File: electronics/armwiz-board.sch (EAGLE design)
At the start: 99 parts, among them IC3 SN74LVC1G74DCT, J1 MICRO-SDCARD-CONNECTOR-330006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, Q1 DMP2035U-7, Q2 DMP2035U-7, Q3 DMN2075U-7, Q4 DMN2075U-7, Q5 DMP2035U-7, U1 STM32F10XRXT6, U2 APX809, U3 MCP73831, U4 MIC5219-3.3V, X1 FH12-12S-1S

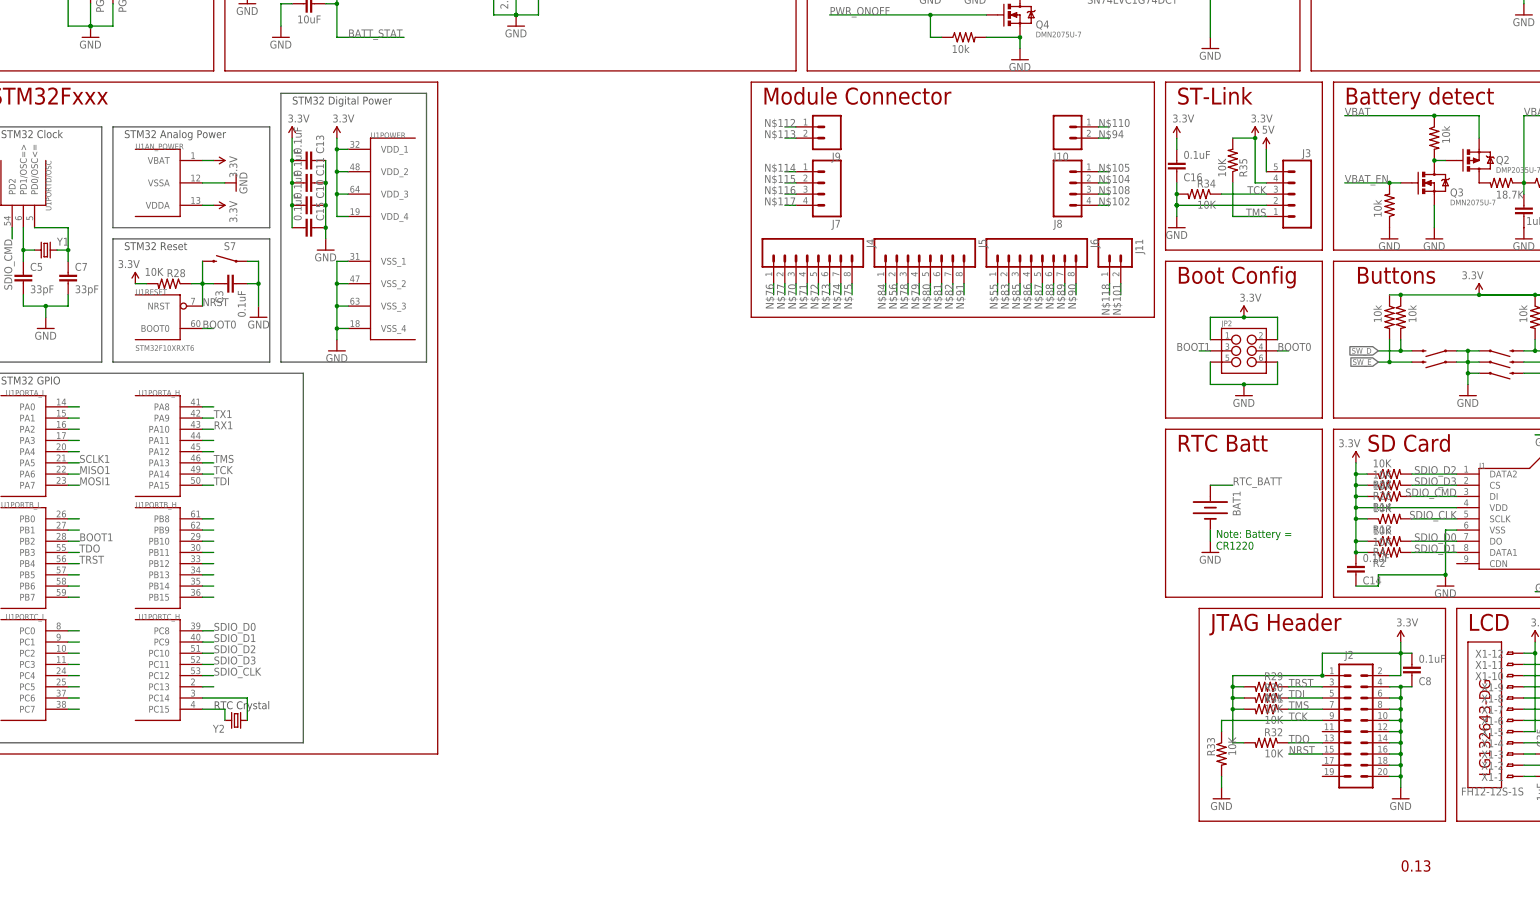
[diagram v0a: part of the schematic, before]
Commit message: Removed JTAG and ST-Link connectors. Added ARM Cortex Debug connector.
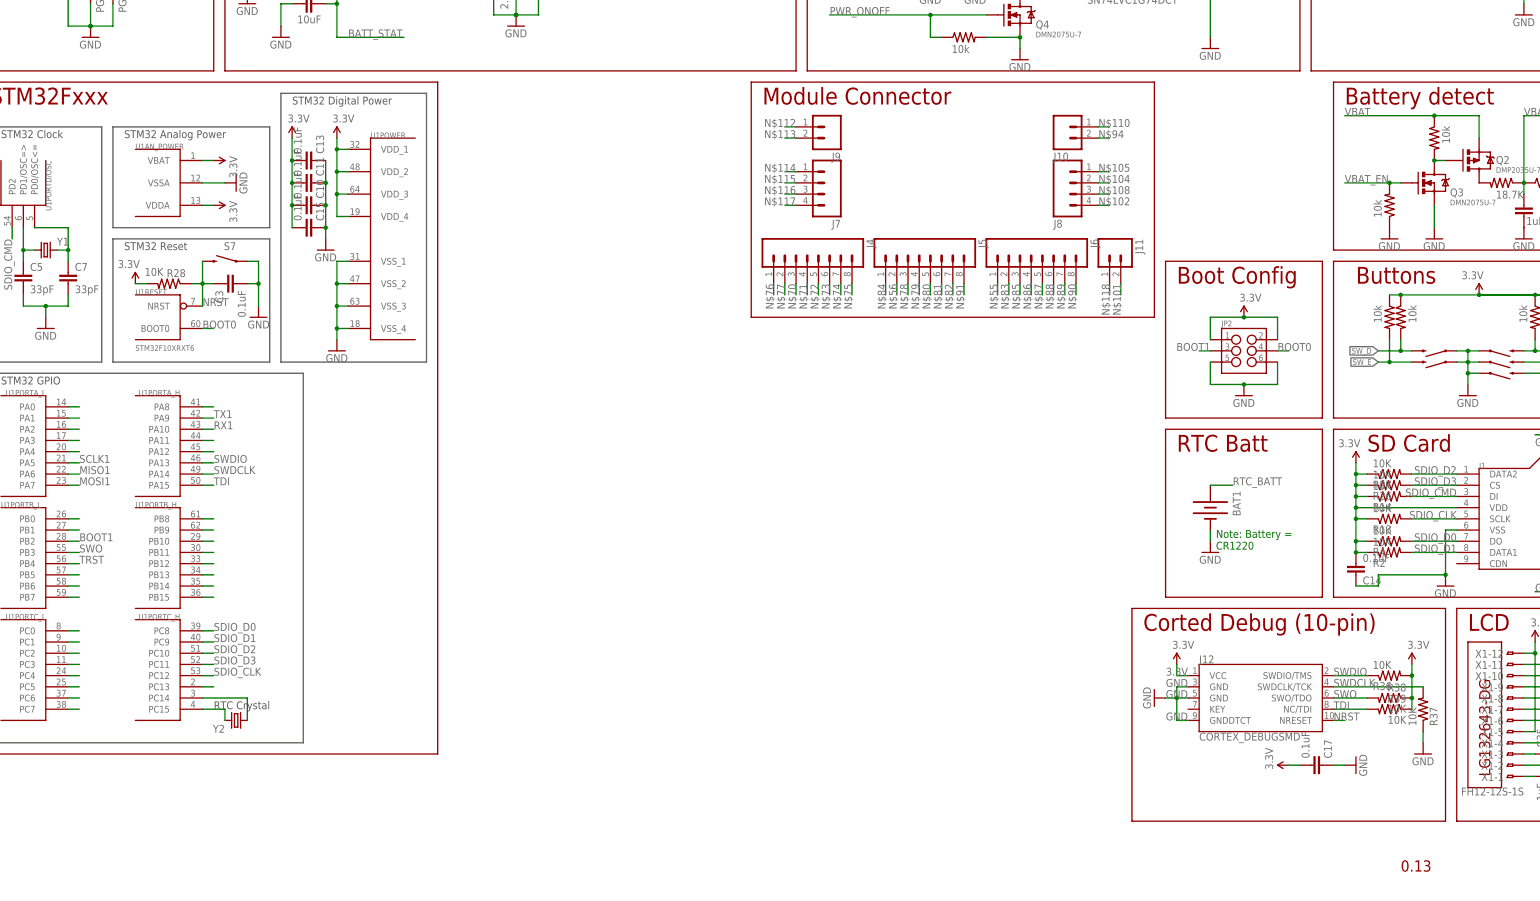
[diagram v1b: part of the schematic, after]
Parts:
- removed C16, C8: 0.1uF, SparkFun-Capacitors:0.1UF-25V-5%(0603)
- removed J2: (no value), SparkFun-Connectors:M10X2
- removed J3: (no value), SparkFun-Connectors:M05PTH
- removed R29, R30, R31, R32, R33, R34, R35: 10K, SparkFun-Resistors:10KOHM-1/10W-1%(0603)0603
- added C17: 0.1uF, SparkFun-Capacitors:0.1UF-25V-5%(0603)
- added J12: CORTEX_DEBUGSMD, SparkFun-Connectors:CORTEX_DEBUGSMD
- added R36, R37, R38, R39: 10K, SparkFun-Resistors:10KOHM-1/10W-1%(0603)0603
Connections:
- removed net 5V: J3.5
- removed net TCK: J2.9, J3.3, R33.1, R34.1, U1PORTA_H.PA14
- removed net TDO: J2.13, R32.1, U1PORTB_L.PB3
- removed net TMS: J2.7, J3.1, R31.1, R35.1, U1PORTA_H.PA13
- new net SWDCLK: J12.SWDCLK/TCK, R37.2, U1PORTA_H.PA14
- new net SWDIO: J12.SWDIO/TMS, R36.1, U1PORTA_H.PA13
- new net SWO: J12.SWO/TDO, R38.2, U1PORTB_L.PB3
- net 3.3V: now also C17.2, J12.VCC, R36.2, R38.1, R39.1; no longer C16.2, C8.2, J2.1, J2.2, J3.4, R29.2, R30.2, R31.2, R32.2, R35.2
- net GND: now also C17.1, J12.GND@3, J12.GND@5, J12.GNDDTCT, R37.1; no longer C16.1, C8.1, J2.10, J2.12, J2.14, J2.16, J2.18, J2.20, J2.4, J2.6, J2.8, J3.2, R33.2, R34.2
- net NRST: now also J12.NRESET; no longer J2.15
- net TDI: now also J12.NC/TDI, R39.2; no longer J2.5, R30.1
- net TRST: no longer J2.3, R29.1
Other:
- note added: "Corted Debug (10-pin)"
- note removed: "JTAG Header"
- note removed: "ST-Link"

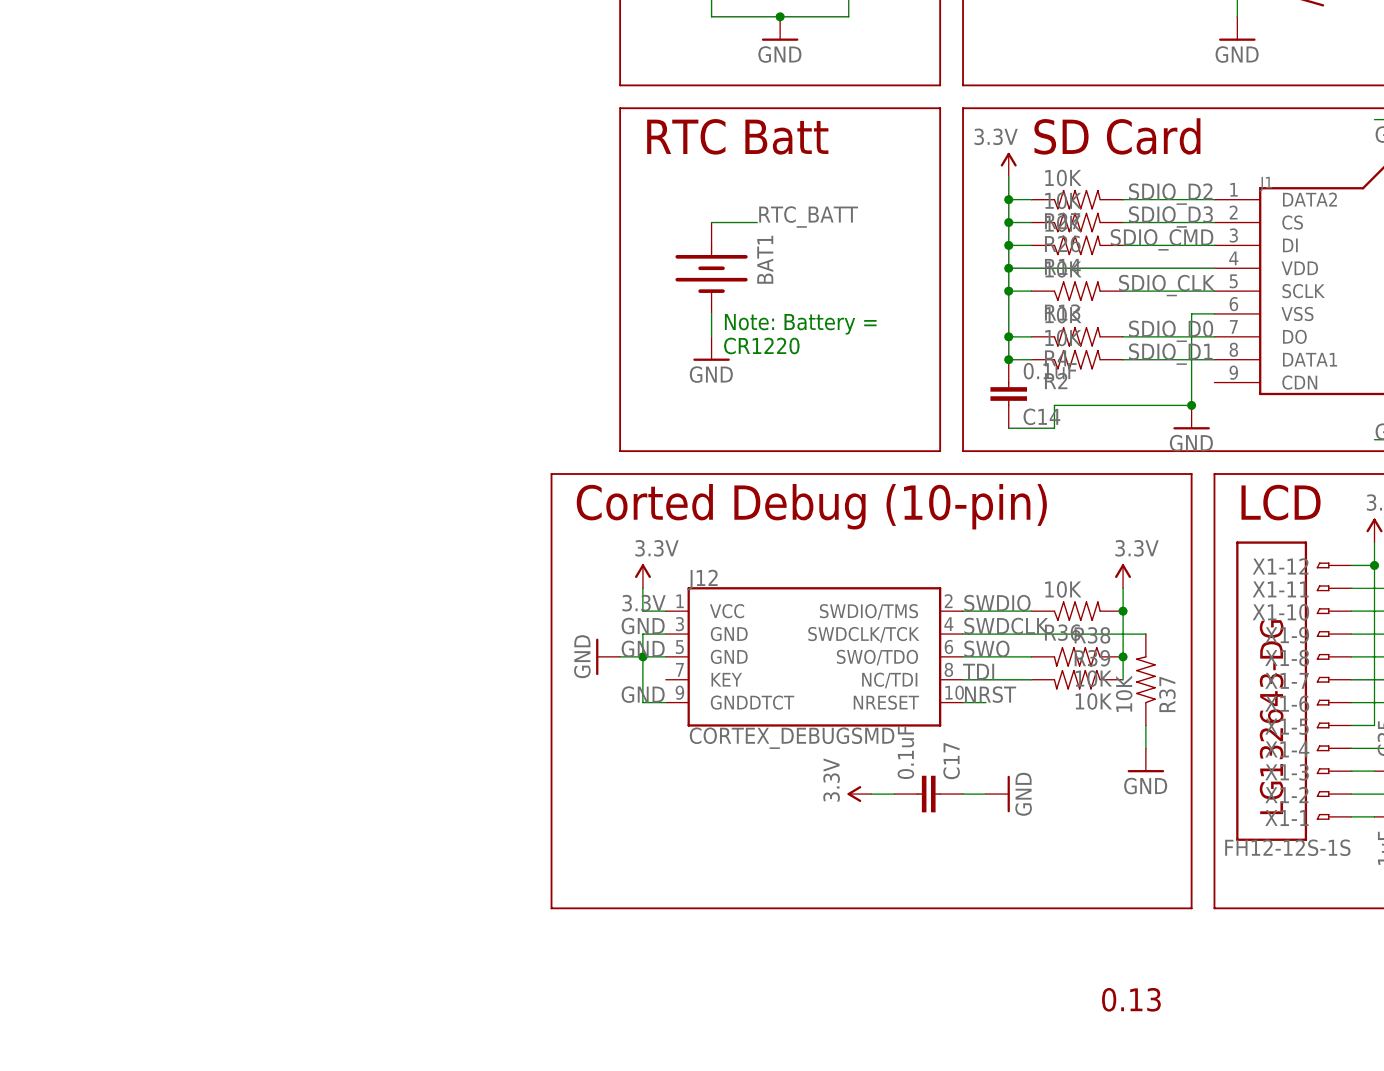
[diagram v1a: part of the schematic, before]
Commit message: Readded the ST Link connection. I'll try to keep them both.
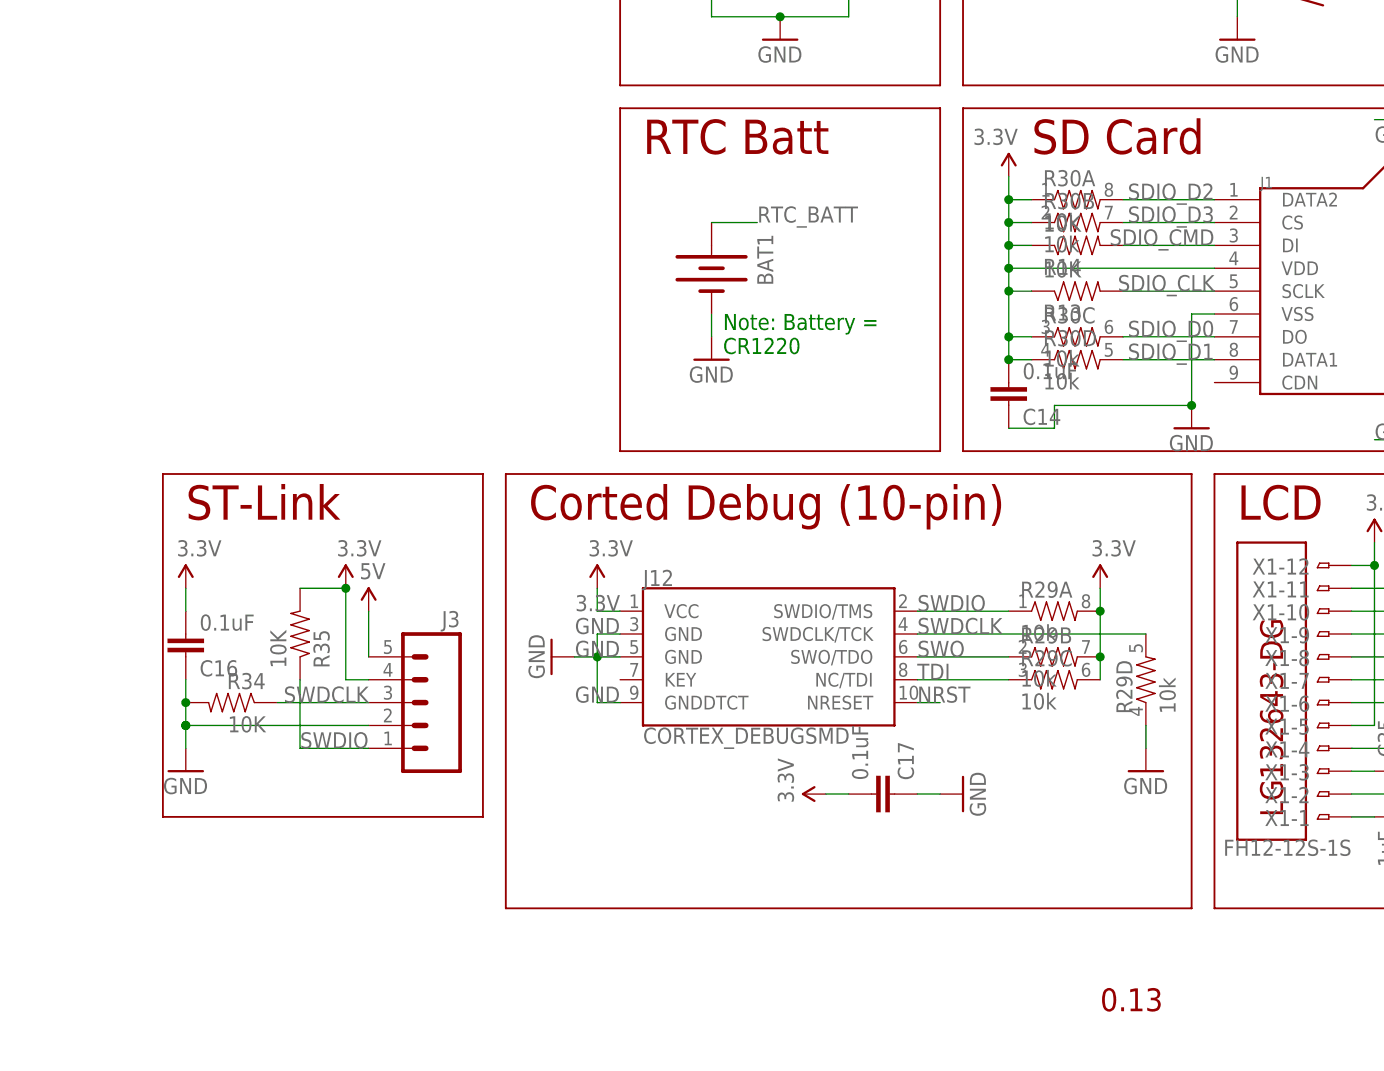
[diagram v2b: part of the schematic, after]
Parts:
- removed R2, R26, R27, R36, R37, R38, R39, R4: 10K, SparkFun-Resistors:10KOHM-1/10W-1%(0603)0603
- added C16: 0.1uF, SparkFun-Capacitors:0.1UF-25V-5%(0603)
- added J3: (no value), SparkFun-Connectors:M05PTH
- added R29, R30: 10k, SparkFun-Passives:RESISTOR-ARRAY0603-ARV
- added R34, R35: 10K, SparkFun-Resistors:10KOHM-1/10W-1%(0603)0603
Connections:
- new net 5V: J3.5
- net 3.3V: now also C16.2, J3.4, R29A.2, R29B.2, R29C.2, R30A.1, R30B.1, R30C.1, R30D.1, R35.2; no longer R2.1, R26.1, R27.1, R36.2, R38.1, R39.1, R4.1
- net GND: now also C16.1, J3.2, R29D.1, R34.2; no longer R37.1
- net SDIO_D0: now also R30C.2; no longer R4.2
- net SDIO_D1: now also R30D.2; no longer R2.2
- net SDIO_D2: now also R30A.2; no longer R27.2
- net SDIO_D3: now also R30B.2; no longer R26.2
- net SWDCLK: now also J3.3, R29D.2, R34.1; no longer R37.2
- net SWDIO: now also J3.1, R29A.1, R35.1; no longer R36.1
- net SWO: now also R29B.1; no longer R38.2
- net TDI: now also R29C.1; no longer R39.2
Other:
- note added: "ST-Link"
- moved on the sheet: C17, J12

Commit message: Cleaned up the schematic. No electrical changes.
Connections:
- removed net N$13: U1PORTC_H.PC15, Y2.2
- removed net N$14: U1PORTC_H.PC14, Y2.1
- removed net N$31: R10.1, U$1.D-, Z2.2
- removed net N$33: R9.1, U$1.D+, Z1.2
- removed net N$35: U1PORTA_H.PA12
- removed net N$36: U1PORTA_H.PA11
- new net RTC1: U1PORTC_H.PC14, Y2.2
- new net RTC2: U1PORTC_H.PC15, Y2.1
- new net USB+: R9.2, U1PORTA_H.PA12
- new net USB-: R10.2, U1PORTA_H.PA11
- net 3.3V: no longer U1AN_POWER.VBAT
- net D+: now also R9.1, U$1.D+, Z1.2; no longer R9.2
- net D-: now also R10.1, U$1.D-, Z2.2; no longer R10.2
- net RTC_BATT: now also U1AN_POWER.VBAT
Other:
- note added: "Real Time Clock"
- note removed: "RTC Batt"
- note removed: "RTC Crystal"
- moved on the sheet: BAT1, C1, C10, C11, C13, C14, C15, C16, C17, C2, C26, C27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

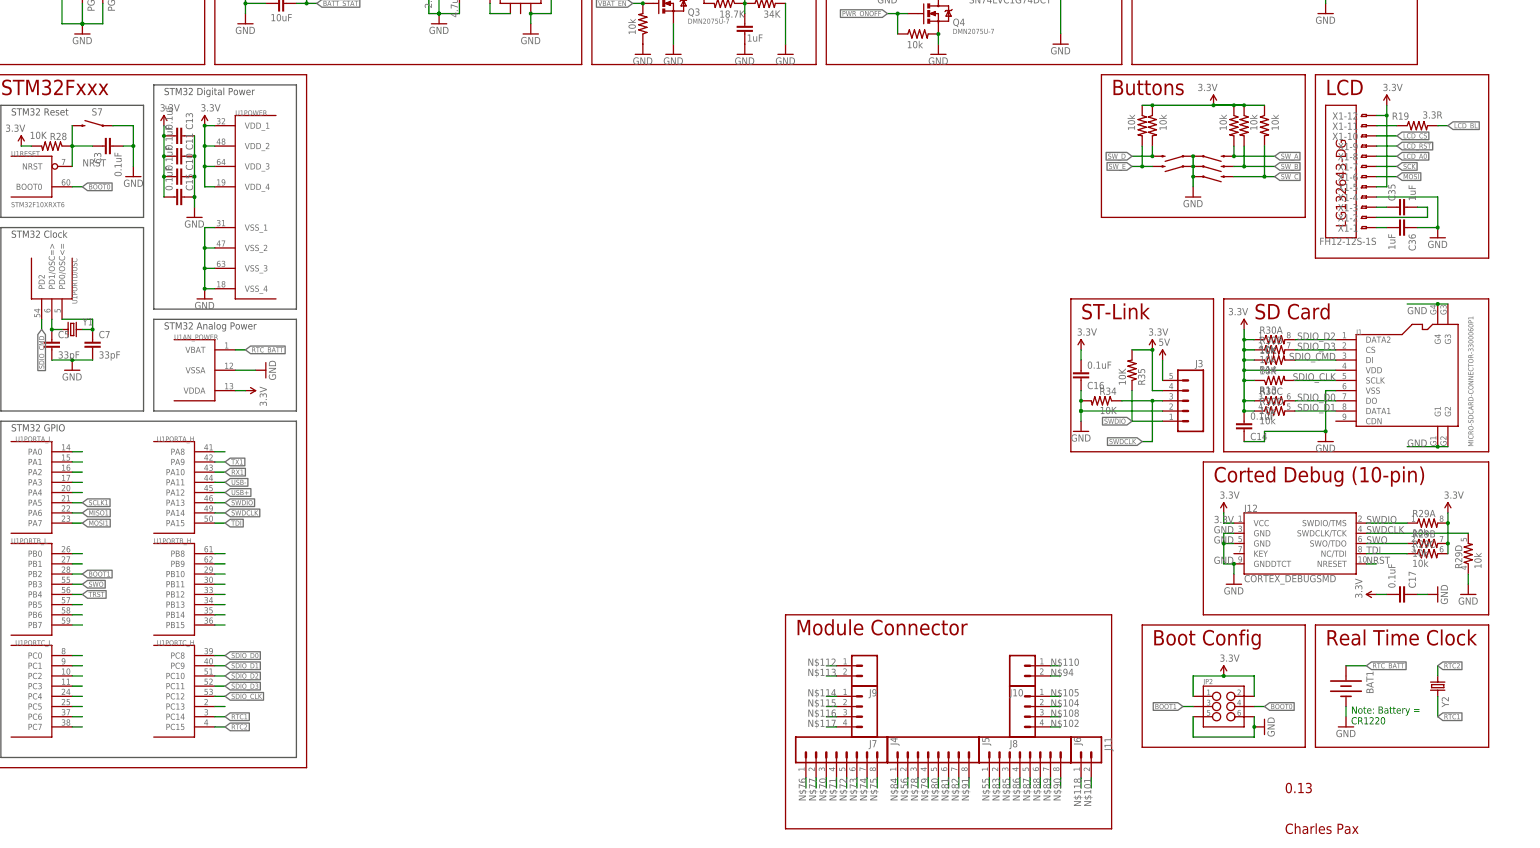
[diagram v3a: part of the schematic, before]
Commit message: Copied labels for all the pins that need to be connected to the MCU.
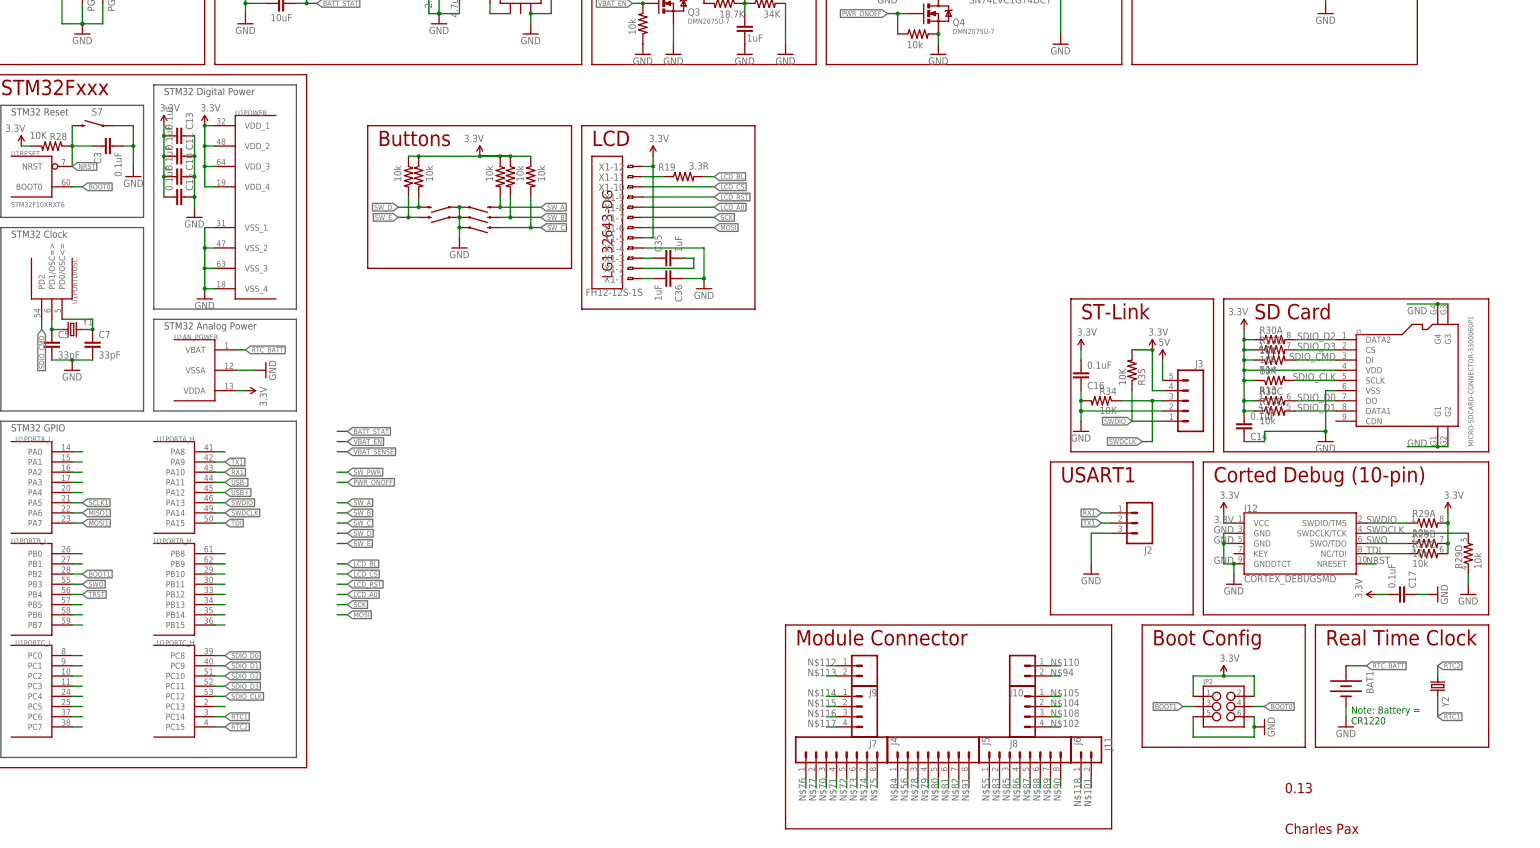
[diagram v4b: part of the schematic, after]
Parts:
- added J2: (no value), SparkFun-Connectors:M031X03_NO_SILK
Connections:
- net GND: now also J2.3
- net RX1: now also J2.1
- net TX1: now also J2.2
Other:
- note added: "USART1"
- moved on the sheet: C35, C36, R19, X1-1, X1-10, X1-11, X1-12, X1-2, X1-3, X1-4, X1-5, X1-6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

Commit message: Added some traces. Just starting layout to see the general areas things should be. Then I can determine where the LCD and other items should be connected to the MCU.
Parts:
- added C8: 0.1uF, SparkFun-Capacitors:0.1UF-25V-5%(0603)
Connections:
- net 3.3V: now also C8.2
- net GND: now also C8.1
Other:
- moved on the sheet: C10, C11, C13, C15, C3, C35, C36, C5, C7, R19, S7, U1AN_POWER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
